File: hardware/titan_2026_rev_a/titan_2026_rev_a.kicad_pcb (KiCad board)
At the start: 2 copper layers, 65 x 56 mm, 73 parts, among them J1 SEC_{OUT}, J10 Conn_02x20_Odd_Even, J2 SEC_{IN}, J3 SWD, J4 BATTERY, J5 MONITOR, J6 DHT, J7 CO_{2}, J8 WHEELS, J9 USB_B_Mini, Q1 DMG2301L, SW1 RPON, SW2 SHTDN, SW3 MCU_RST, U1 NRF24L01, U2 AP62301WU, U3 ULT-GPS, U4 STM32F103C8Tx, Y1 8MHz

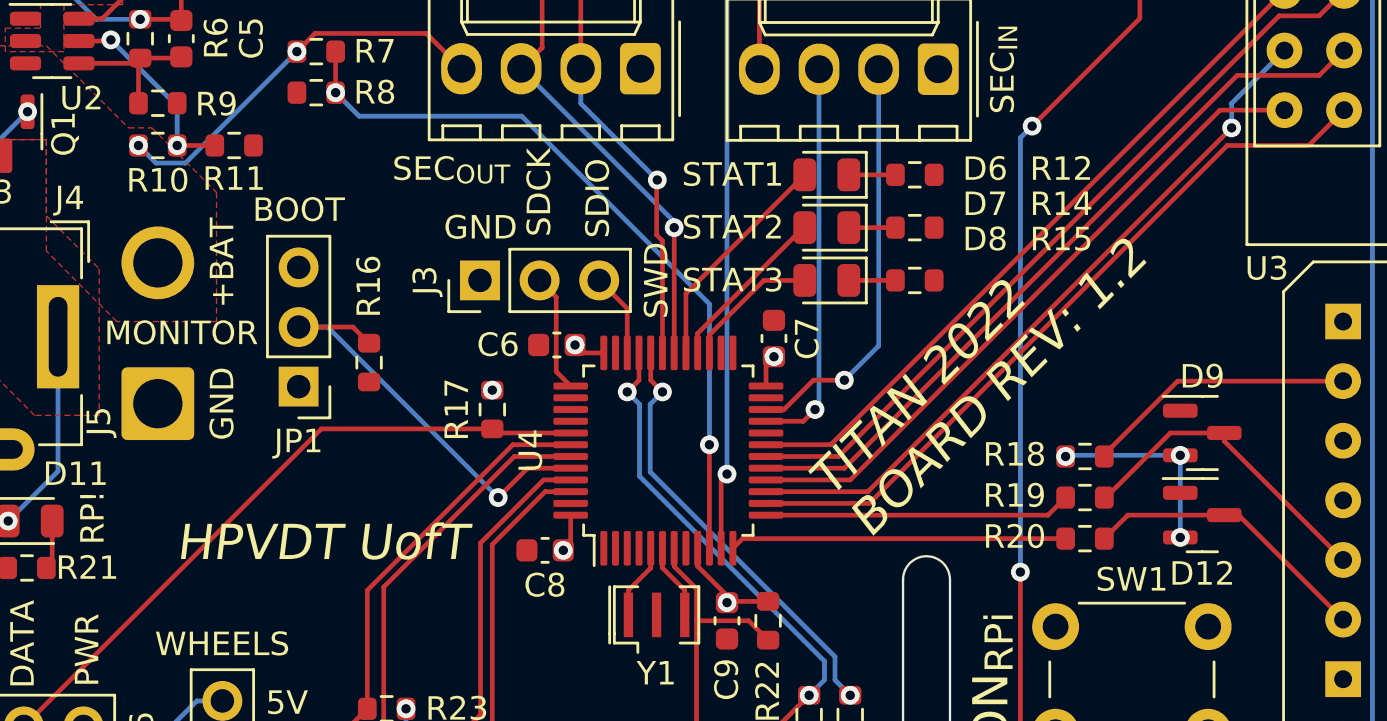
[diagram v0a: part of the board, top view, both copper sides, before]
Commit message: Brought KiCad projects into KiCad 10.0
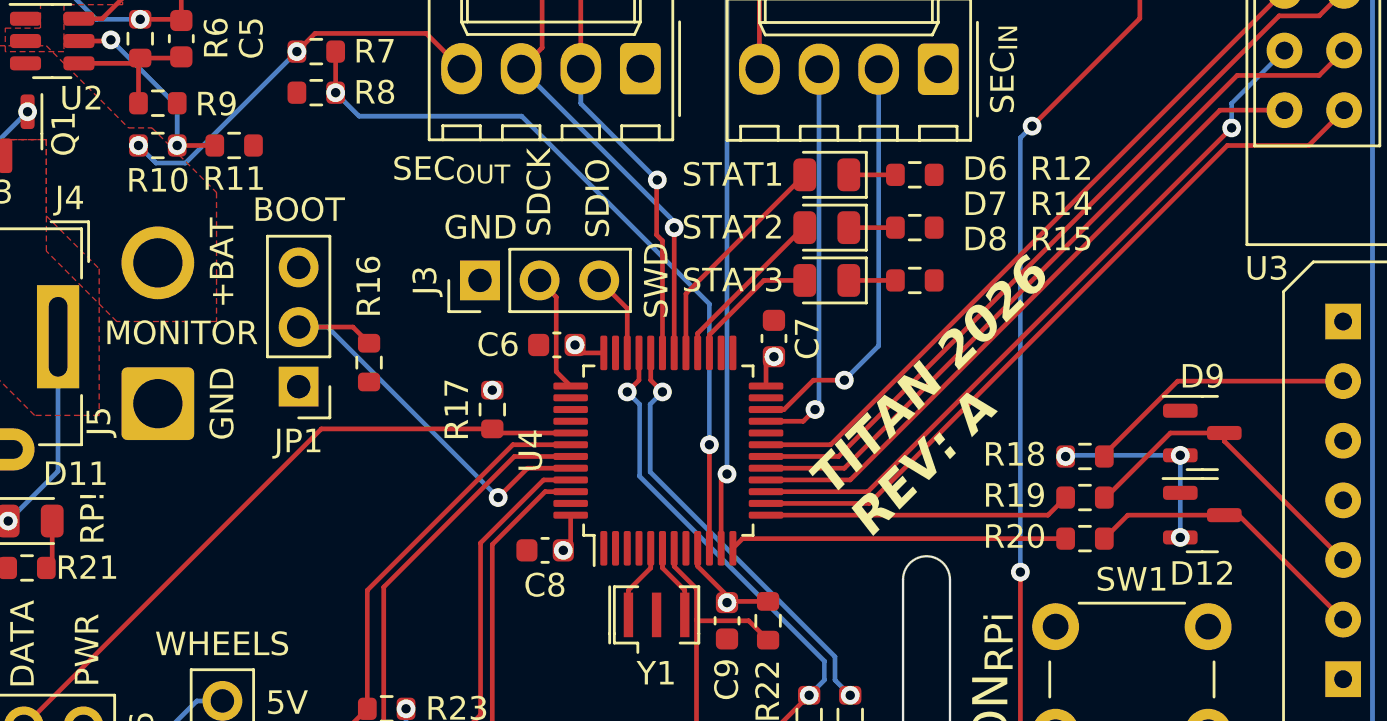
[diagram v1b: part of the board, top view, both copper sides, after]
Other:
- board text added: "TITAN 2026 REV: ${REVISION}"
- board text removed: "HPVDT UofT"
- board text removed: "TITAN 2022 BOARD REV: ${REVISION}"

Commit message: Completed rev A schematics
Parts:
- removed J5: MONITOR, Connector_Wire:SolderWire-1.5sqmm_1x02_P6mm_D1.7mm_OD3mm
- added BT1: Battery, Connector_AMASS:AMASS_XT30PW-M_1x02_P2.50mm_Horizontal, F.Cu at (120.0, 128.1)
- J4: value BATTERY -> Conn_01x02; footprint Connector_BarrelJack:BarrelJack_Wuerth_6941xx301002 -> Connector_AMASS:AMASS_XT30PW-F_1x02_P2.50mm_Horizontal
- moved J4 52.1 mm to (99.7, 129.1), turned to 0 degrees
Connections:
- J4 pad 1: /BATT_{IN+} -> GND
- J4 pad 2: GND -> +BATT

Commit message: Drafted initial floor plan of rev A
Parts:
- removed BT1: Battery, Connector_AMASS:AMASS_XT30PW-M_1x02_P2.50mm_Horizontal
- removed the C4 at (93.8, 65.3)
- removed the C5 at (103.0, 64.3)
- removed D10: BAV70, Package_TO_SOT_SMD:SOT-23
- removed D11: RP, Diode_SMD:D_0805_2012Metric
- removed D12, D9: TBAT54S, Package_TO_SOT_SMD:SOT-23
- removed D4, D6, D7, D8: LED, LED_SMD:LED_0805_2012Metric
- removed D5: 5V6, Diode_SMD:D_SOD-323
- removed the J1 at (122.6, 65.6)
- removed Q1: DMG2301L, Package_TO_SOT_SMD:SOT-23
- removed R25: 22, Resistor_SMD:R_0603_1608Metric
- removed R26: 2k, Resistor_SMD:R_0603_1608Metric
- removed R27: 10k, Resistor_SMD:R_0603_1608Metric
- removed SW2: SHTDN, Button_Switch_THT:SW_PUSH_6mm_H4.3mm
- removed SW3: MCU_RST, Button_Switch_THT:SW_PUSH_6mm_H4.3mm
- added C11: 100n, Capacitor_SMD:C_0402_1005Metric, F.Cu at (93.2, 65.5)
- added C12: 10u, Capacitor_SMD:C_0603_1608Metric, F.Cu at (118.0, 82.5)
- added C13: 100n, Capacitor_SMD:C_0402_1005Metric, F.Cu at (116.0, 87.8)
- added C14: 22u, Capacitor_SMD:C_0603_1608Metric, F.Cu at (127.5, 83.8)
- added C15: 22u, Capacitor_SMD:C_0603_1608Metric, F.Cu at (127.5, 87.2)
- added C16: 10u, Capacitor_SMD:C_0603_1608Metric, F.Cu at (105.5, 61.0)
- added C17: 10u, Capacitor_SMD:C_0603_1608Metric, F.Cu at (92.5, 74.5)
- added C18: 100n, Capacitor_SMD:C_0402_1005Metric, F.Cu at (89.5, 89.5)
- added C19: 470p, Capacitor_SMD:C_0402_1005Metric, F.Cu at (89.0, 94.5)
- added C20: 100n, Capacitor_SMD:C_0402_1005Metric, F.Cu at (123.0, 60.0)
- added C21: 100n, Capacitor_SMD:C_0402_1005Metric, F.Cu at (137.0, 60.0)
- added C22: 100n, Capacitor_SMD:C_0402_1005Metric, F.Cu at (109.5, 84.5)
- added C23: 100n, Capacitor_SMD:C_0402_1005Metric, F.Cu at (91.8, 59.5)
- added C8: 100n, Capacitor_SMD:C_0402_1005Metric, F.Cu at (111.8, 60.2)
- added C9: 100n, Capacitor_SMD:C_0402_1005Metric, F.Cu at (109.5, 87.5)
- added J10: XT30PW-F30.G.Y, Connector_AMASS:AMASS_XT30PW-F_1x02_P2.50mm_Horizontal, F.Cu at (129.0, 91.8)
- added J11: XT30PW-M30.G.Y, Connector_AMASS:AMASS_XT30PW-M_1x02_P2.50mm_Horizontal, F.Cu at (108.2, 92.8)
- added J12: BWSMA-KWE-Z001, Connector_Coaxial:SMA_BAT_Wireless_BWSMA-KWE-Z001, F.Cu at (83.5, 94.5)
- added J5: B3B-XH, Connector_JST:JST_XH_B3B-XH-A_1x03_P2.50mm_Vertical, F.Cu at (149.0, 83.0)
- added JP2: SolderJumper_3_Open, Jumper:SolderJumper-3_P2.0mm_Open_TrianglePad1.0x1.5mm, F.Cu at (110.2, 78.2)
- added JP3: SolderJumper_3_Open, Jumper:SolderJumper-3_P2.0mm_Open_TrianglePad1.0x1.5mm_NumberLabels, F.Cu at (119.5, 102.2)
- added JP4: SolderJumper_2_Open, Jumper:SolderJumper-2_P1.3mm_Open_Pad1.0x1.5mm, F.Cu at (130.0, 71.0)
- added L2: 6n8, Inductor_SMD:L_0402_1005Metric, F.Cu at (91.0, 94.0)
- added U10: TPS2116DRL, Package_TO_SOT_SMD:SOT-583-8, F.Cu at (130.7, 86.0)
- added U11: ATGM336H-5N31, titan:ATGM336H-5N, F.Cu at (95.5, 82.0)
- added U12: NRF24L01_Breakout, titan:nRF24L01_PA_LNA_Breakout, F.Cu at (103.0, 60.0)
- added U13: AT2659S, Package_TO_SOT_SMD:SOT-23-6, F.Cu at (92.0, 90.5)
- added U5: USBLC6-2SC6, Package_TO_SOT_SMD:SOT-23-6, F.Cu at (141.5, 95.0)
- added U6: INA219AIDCN, Package_SO:SOIC-8_3.9x4.9mm_P1.27mm, F.Cu at (105.0, 86.0)
- added U7: TLV73333PDBV, Package_TO_SOT_SMD:SOT-23-5, F.Cu at (91.8, 62.5)
- added U8: TPS563201, Package_TO_SOT_SMD:SOT-23-6, F.Cu at (117.0, 85.2)
- added U9: TPS2116DRL, Package_TO_SOT_SMD:SOT-583-8, F.Cu at (93.5, 67.5)
- C1: footprint Capacitor_SMD:C_0603_1608Metric -> Capacitor_SMD:C_0402_1005Metric
- C2, C3: value 22u -> 100n; footprint Capacitor_SMD:C_0805_2012Metric -> Capacitor_SMD:C_0402_1005Metric
- C4: renamed from C8; footprint Capacitor_SMD:C_0603_1608Metric -> Capacitor_SMD:C_0402_1005Metric
- C5: renamed from C6; footprint Capacitor_SMD:C_0603_1608Metric -> Capacitor_SMD:C_0402_1005Metric
- C6: renamed from C7; footprint Capacitor_SMD:C_0603_1608Metric -> Capacitor_SMD:C_0402_1005Metric
- C7: renamed from C9; footprint Capacitor_SMD:C_0603_1608Metric -> Capacitor_SMD:C_0402_1005Metric
- D1: value TBAT54S -> RED; footprint Package_TO_SOT_SMD:SOT-23 -> LED_SMD:LED_0805_2012Metric
- D2, D3: value TBAT54S -> WHITE; footprint Package_TO_SOT_SMD:SOT-23 -> LED_SMD:LED_0805_2012Metric
- J1: renamed from J10; value Conn_02x20_Odd_Even -> DS1023-2*20SF11
- J2: value SEC_{IN} -> B5B-XH; footprint Connector_Molex:Molex_KK-254_AE-6410-04A_1x04_P2.54mm_Vertical -> Connector_JST:JST_XH_B5B-XH-A_1x05_P2.50mm_Vertical
- J3: value SWD -> B5B-XH; footprint Connector_PinHeader_2.54mm:PinHeader_1x03_P2.54mm_Vertical -> Connector_JST:JST_XH_B5B-XH-A_1x05_P2.50mm_Vertical
- J4: value Conn_01x02 -> B3B-XH; footprint Connector_AMASS:AMASS_XT30PW-F_1x02_P2.50mm_Horizontal -> Connector_JST:JST_XH_B3B-XH-A_1x03_P2.50mm_Vertical
- J6: value DHT -> HB-PH9-12727PB2GOB; footprint Connector_PinHeader_2.54mm:PinHeader_1x03_P2.54mm_Vertical -> Connector_PinHeader_1.27mm:PinHeader_2x07_P1.27mm_Vertical_SMD
- J7: value CO_{2} -> B7B-XH; footprint Connector_PinHeader_2.54mm:PinHeader_1x03_P2.54mm_Vertical -> Connector_JST:JST_XH_B7B-XH-A_1x07_P2.50mm_Vertical
- J8: value WHEELS -> B7B-XH; footprint Connector_PinHeader_2.54mm:PinHeader_1x05_P2.54mm_Vertical -> Connector_JST:JST_XH_B7B-XH-A_1x07_P2.50mm_Vertical
- J9: value USB_B_Mini -> USB4105-GF-A-120; footprint 2172034-1:TE_2172034-1 -> Connector_USB:USB_C_Receptacle_GCT_USB4105-xx-A_16P_TopMnt_Horizontal
- JP1: value BOOT0 -> SolderJumper_3_Open; footprint Connector_PinHeader_2.54mm:PinHeader_1x03_P2.54mm_Vertical -> Jumper:SolderJumper-3_P2.0mm_Open_TrianglePad1.0x1.5mm
- L1: footprint Inductor_SMD:L_Taiyo-Yuden_NR-50xx -> Inductor_SMD:L_Changjiang_FNR6045S
- R1, R12, R14: value 330 -> 120; footprint Resistor_SMD:R_0603_1608Metric -> Resistor_SMD:R_0402_1005Metric
- R10: value 97k6 -> 5k1; footprint Resistor_SMD:R_0603_1608Metric -> Resistor_SMD:R_0402_1005Metric
- R11: value 13k3 -> 5k1; footprint Resistor_SMD:R_0603_1608Metric -> Resistor_SMD:R_0402_1005Metric
- R13: value 10k -> 10m; footprint Resistor_SMD:R_0603_1608Metric -> Resistor_SMD:R_0805_2012Metric
- R15: value 330 -> 2k; footprint Resistor_SMD:R_0603_1608Metric -> Resistor_SMD:R_0402_1005Metric
- R16, R17, R8, R9: value 10k -> 2k; footprint Resistor_SMD:R_0603_1608Metric -> Resistor_SMD:R_0402_1005Metric
- R18, R22, R3: value 10k -> 28k; footprint Resistor_SMD:R_0603_1608Metric -> Resistor_SMD:R_0402_1005Metric
- R19, R20: value 2k -> 5k1; footprint Resistor_SMD:R_0603_1608Metric -> Resistor_SMD:R_0402_1005Metric
- R2, R4: value 2k -> 120; footprint Resistor_SMD:R_0603_1608Metric -> Resistor_SMD:R_0402_1005Metric
- R21, R23: footprint Resistor_SMD:R_0603_1608Metric -> Resistor_SMD:R_0402_1005Metric
- R24: value 22 -> 2k; footprint Resistor_SMD:R_0603_1608Metric -> Resistor_SMD:R_0402_1005Metric
- R5: value 52k3 -> 5k1; footprint Resistor_SMD:R_0603_1608Metric -> Resistor_SMD:R_0402_1005Metric
- R6, R7: value 52k3 -> 2k; footprint Resistor_SMD:R_0603_1608Metric -> Resistor_SMD:R_0402_1005Metric
- SW1: value RPON -> SW_SPST; footprint Button_Switch_THT:SW_PUSH_6mm_H4.3mm -> titan:SW_SPST_SKPM
- U1: value NRF24L01 -> BME280; footprint RF_Module:nRF24L01_Breakout -> Package_LGA:Bosch_LGA-8_2.5x2.5mm_P0.65mm_ClockwisePinNumbering
- U2: value AP62301WU -> SCD41-D-R2; footprint Package_TO_SOT_SMD:TSOT-23-6 -> Sensor:Sensirion_SCD4x-1EP_10.1x10.1mm_P1.25mm_EP4.8x4.8mm
- U3: value ULT-GPS -> STM32F105RCT6; footprint ultimate_gps:ULT-GPS -> Package_QFP:LQFP-64_10x10mm_P0.5mm
- U4: value STM32F103C8Tx -> ISO1642DWR; footprint Package_QFP:LQFP-48_7x7mm_P0.5mm -> Package_SO:SOIC-16W_7.5x10.3mm_P1.27mm
- Y1: value 8MHz -> 8M; footprint Crystal:Resonator_SMD_Murata_CSTxExxV-3Pin_3.0x1.1mm -> Crystal:Crystal_SMD_2520-4Pin_2.5x2.0mm
- moved U1 85.4 mm to (76.2, 102.8), turned to 180 degrees
- moved SW1 65.9 mm to (84.0, 55.0), turned to 180 degrees
- moved J8 60.4 mm to (149.0, 61.5), turned to -90 degrees
- moved J4 58.2 mm to (140.9, 88.0), turned to 90 degrees
- moved J7 51.6 mm to (141.0, 76.5)
- moved J2 48.9 mm to (86.5, 62.0), turned to -90 degrees
- moved R11 48.3 mm to (144.5, 97.0)
- moved C1 47.2 mm to (75.2, 100.4), turned to 0 degrees
- moved R10 46.1 mm to (138.5, 97.0), turned to 0 degrees
- moved R23 45.2 mm to (153.0, 74.2), turned to -90 degrees
- moved J6 42.4 mm to (133.2, 78.2), turned to 0 degrees
- moved C2 40.4 mm to (77.2, 100.4), turned to 180 degrees
- moved R15 39.1 mm to (96.0, 66.5), turned to 0 degrees
- moved R22 38.0 mm to (153.0, 60.5)
- moved U3 37.9 mm to (115.2, 69.2), turned to -90 degrees
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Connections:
- C1 pad 1: /SW -> +3V3
- C1 pad 2: /BST -> GND
- C2 pad 1: +5V -> +3V3
- C3 pad 1: +5V -> GND
- C3 pad 2: GND -> +3V3
- D1 pad 2: +3V3 -> Net-(D1-A)
- D2 pad 2: +3V3 -> Net-(D2-A)
- D3 pad 2: +3V3 -> Net-(D3-A)
- J1 pad 1: +3V3 -> +3V3_RPI
- J1 pad 10: /GPIO15(RXD0) -> /RPI_{RX}
- J1 pad 15: unconnected-(J10-Pin_15-Pad15) -> /ROLE
- J1 pad 17: +3V3 -> +3V3_RPI
- J1 pad 37: /GPIO26 -> unconnected-(J1-GPIO26-Pad37)
- J1 pad 5: /GPIO3(SCL1) -> /RPI_SW
- J1 pad 8: /GPIO14(TXD0) -> /RPI_{TX}
- J2 pad 1: GND -> +5V
- J2 pad 2: /SEC_{TX} -> /SCL_{WHL}
- J2 pad 3: /SEC_{RX} -> /SDA_{WHL}
- J2 pad 4: /SEC_{BATT} -> /ENC_FRONT
- J3 pad 1: GND -> +5V
- J3 pad 2: /SWCLK -> /SCL_{WHL}
- J3 pad 3: /SDWIO -> /SDA_{WHL}
- J4 pad 1: GND -> +5V
- J4 pad 2: +BATT -> /CO_{2}
- J6 pad 1: GND -> unconnected-(J6-NC-Pad1)
- J6 pad 2: /DHT_{DATA} -> unconnected-(J6-NC-Pad2)
- J7 pad 1: GND -> /Interboard Comms/SCL_{ISO}
- J7 pad 2: /CO_{2} -> /Interboard Comms/SDA_{ISO}
- J7 pad 3: +5V -> /Interboard Comms/3V3_{ISO}
- J8 pad 1: GND -> /RPI_{TX}
- J8 pad 2: /ENCODER -> /RPI_{RX}
- J8 pad 3: /SDA -> /ROLE
- J8 pad 4: /SCL -> GND
- J8 pad 5: +5V -> +3V3
- JP1 pad 1: GND -> /SCL
- JP1 pad 2: /BOOT0 -> /Power/SDA
- JP1 pad 3: +3V3 -> /SCL_{SEC}
- L1 pad 1: /SW -> Net-(U8-SW)
- L1 pad 2: +5V -> /Power/5V_REG
- R1 pad 1: GND -> Net-(D1-A)
- R1 pad 2: Net-(D4-K) -> /STATUS_{1}
- R10 pad 1: /EN_{5V} -> GND
- R10 pad 2: +BATT -> Net-(J9-CC1)
- R11 pad 2: /EN_{5V} -> Net-(J9-CC2)
- R12 pad 1: GND -> Net-(J11-Pin_2)
- R13 pad 1: GND -> Net-(J11-Pin_2)
- R13 pad 2: /RP_{G} -> +BATT
- R14 pad 1: GND -> +BATT
- R15 pad 1: GND -> +3V3_RPI
- R15 pad 2: Net-(D8-K) -> Net-(R15-Pad2)
- R16 pad 1: GND -> Net-(R15-Pad2)
- R16 pad 2: /BOOT0 -> Net-(U9-PR1)
- R17 pad 1: /DHT_{DATA} -> Net-(U9-PR1)
- R17 pad 2: +3V3 -> GND
- R18 pad 1: /GPS_{EN} -> /Power/5V_REG
- R18 pad 2: +3V3 -> Net-(U8-VFB)
- R19 pad 1: /GPS_{TX} -> GND
- R19 pad 2: /GPS_{tx} -> Net-(U8-VFB)
- R2 pad 1: /RPI_{RX} -> Net-(D2-A)
- R2 pad 2: /GPIO15(RXD0) -> /STATUS_{2}
- R20 pad 1: /GPS_{RX} -> Net-(U10-PR1)
- R20 pad 2: /GPS_{rx} -> /Power/5V_REG
- R21 pad 1: Net-(D10-K) -> Net-(U10-PR1)
- R21 pad 2: Net-(D11-A) -> GND
- R22 pad 1: /RST -> /ROLE
- R22 pad 2: +3V3 -> GND
- R23 pad 1: +5V -> +3V3
- R23 pad 2: /SCL -> /SDA_{SEC}
- R24 pad 1: /D+ -> +3V3
- R24 pad 2: /d+ -> /SCL_{SEC}
- R3 pad 1: GND -> +3V3
- R3 pad 2: /SEC_{LVL} -> /~{RST}
- R4 pad 1: /RPI_{TX} -> Net-(D3-A)
- R4 pad 2: /GPIO14(TXD0) -> /STATUS_{3}
- R5 pad 1: /SEC_{LVL} -> /DHT_{DATA}
- R5 pad 2: /SEC_{BATT} -> +3V3
- R6 pad 1: /FEEDBACK -> +5V
- R6 pad 2: +5V -> /SCL_{WHL}
- R7 pad 1: /BATT_{LVL} -> +5V
- R7 pad 2: +BATT -> /SDA_{WHL}
- R8 pad 1: GND -> +3V3
- R8 pad 2: /BATT_{LVL} -> /SCL
- R9 pad 1: GND -> +3V3
- R9 pad 2: /FEEDBACK -> /SDA
- SW1 pad 1: GND -> /RPI_SW
- SW1 pad 2: /GPIO3(SCL1) -> GND
- U1 pad 3: /RF_{EN} -> /SDA
- U1 pad 4: /RF_{SEL} -> /SCL
- U1 pad 5: /SCK -> +3V3
- U1 pad 6: /MOSI -> +3V3
- U1 pad 7: /MISO -> GND
- U1 pad 8: /RF_{INT} -> +3V3
- U2 pad 1: GND -> (no net)
- U2 pad 2: /SW -> (no net)
- U2 pad 3: +BATT -> (no net)
- U2 pad 4: /FEEDBACK -> (no net)
- U2 pad 5: /EN_{5V} -> (no net)
- U2 pad 6: /BST -> GND
- U3 pad 1: unconnected-(U3-3V3_{INT}-Pad1) -> +3V3
- U3 pad 2: /GPS_{EN} -> unconnected-(U3-PC13-Pad2)
- U3 pad 4: unconnected-(U3-FIX-Pad4) -> /ROLE
- U3 pad 5: /GPS_{tx} -> Net-(U3-PD0)
- U3 pad 6: /GPS_{rx} -> unconnected-(U3-PD1-Pad6)
- U3 pad 7: GND -> /~{RST}
- U3 pad 8: +3V3 -> unconnected-(U3-PC0-Pad8)
- U4 pad 1: unconnected-(U4-VBAT-Pad1) -> +3V3
- U4 pad 10: /BATT_{LVL} -> unconnected-(U4-NC-Pad10)
- U4 pad 11: /SEC_{LVL} -> /Interboard Comms/SCL_{ISO}
- U4 pad 12: /GPS_{RX} -> /Interboard Comms/TX_{ISO}
- U4 pad 13: /GPS_{TX} -> /Interboard Comms/RX_{ISO}
- U4 pad 14: /RF_{INT} -> /Interboard Comms/SDA_{ISO}
- U4 pad 15: /SCK -> unconnected-(U4-NC-Pad15)
- U4 pad 16: /MISO -> /Interboard Comms/3V3_{ISO}
- U4 pad 3: unconnected-(U4-PC14-Pad3) -> /SDA
- U4 pad 4: unconnected-(U4-PC15-Pad4) -> /SEC_{RX}
- U4 pad 5: Net-(U4-PD0) -> /SEC_{TX}
- U4 pad 6: Net-(U4-PD1) -> /SCL
- U4 pad 7: /RST -> unconnected-(U4-NC-Pad7)
- U4 pad 9: +3V3 -> /Interboard Comms/GND_{ISO}
- Y1 pad 1: Net-(U4-PD0) -> +3V3
- Y1 pad 3: Net-(U4-PD1) -> Net-(U3-PD0)
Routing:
- net +5V: track 104.0 -> 0.00 mm, vias 6 -> 0
- net /GPIO3(SCL1): track 102.7 -> 0.00 mm
- net /GPIO26: track 57.7 -> 0.00 mm, vias 2 -> 0
- net /CO_{2}: track 34.8 -> 0.00 mm
- net /SEC_{LVL}: track 33.2 -> 0.00 mm, vias 2 -> 0
- net /RF_{SEL}: track 32.8 -> 0.00 mm
- net /MOSI: track 32.0 -> 0.00 mm
- net /BATT_{LVL}: track 31.8 -> 0.00 mm, vias 2 -> 0
- net /RF_{INT}: track 31.6 -> 0.00 mm
- net /SCK: track 30.5 -> 0.00 mm, vias 1 -> 0
- net /RF_{EN}: track 30.1 -> 0.00 mm
- net /DHT_{DATA}: track 28.6 -> 0.00 mm
- net /MISO: track 28.6 -> 0.00 mm
- net /ENCODER: track 26.4 -> 0.00 mm
- net /RST: track 25.2 -> 0.00 mm
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- removed copper zone on F.Cu, net +5V
- removed copper zone on F.Cu, net +BATT
- removed copper zone on F.Cu, net /BATT_{IN+}
- removed copper zone on F.Cu, net /SW
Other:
- board size 65 x 56 mm -> 82 x 56 mm
- board text added: "Avoiding heating from rest of PCB with rule block"
- board text added: "BATT"
- board text added: "FRNT"
- board text added: "GND TIE"
- board text added: "GPS"
- board text added: "PRIM"
- board text added: "PRIM_{IN}"
- board text added: "PWR_{RPi}"
- board text added: "REAR"
- board text added: "SEC"
- board text removed: "+BAT"
- board text removed: "- Encoder based speed/distance - GPS based speed/distance - Battery levels - CO_{2} levels - Brake temperatures - Ambient temp. / humidity - Rider cadence, heart rate, power"
- board text removed: "BOOT"
- board text removed: "Complete assembly needed only for main screen. Only power supply and {dblquote}SEC_{OUT}{dblquote} header needed on secondary HAT."
- board text removed: "DATA"
- board text removed: "Data collected:"
- board text removed: "JLCJLCJLCJLC"
- board text removed: "OFF_{RPi}"
- board text removed: "ON_{RPi}"
- board text removed: "PWR"
- board text removed: "RP!"
- board text removed: "RST_{MCU}"
- board text removed: "SB"
- board text removed: "SDCK"
- board text removed: "SDIO"
- board text removed: "SEC_{IN}"
- board text removed: "STM32 centered HAT for TITAN. Provides power from battery with UVLO and reverse polarity protection. All data on TITAN passes through the STM32 by UART. Telemetry provided by nRF24L01 module."
- board text removed: "SWD"
- board text removed: "Sec. SEC_{OUT} to main's SEC_{IN} pin-pin!"
- board text removed: "TITAN 2022 RPi HAT"
- board text removed: "TITAN 2026 REV: ${REVISION}"

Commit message: Completed initial layout of rev A
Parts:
- removed H1, H2, H3, H4: M2.5, MountingHole:MountingHole_2.7mm_M2.5
- added MH1: MountingHole_2.7mm_M2.5_ISO14580_Pad_TopBottom, MountingHole:MountingHole_2.7mm_M2.5_ISO14580_Pad_TopBottom, F.Cu at (93.2, 53.8)
- added MH3: MountingHole_2.7mm_M2.5_ISO14580_Pad_TopBottom, MountingHole:MountingHole_2.7mm_M2.5_ISO14580_Pad_TopBottom, F.Cu at (93.2, 102.8)
- added MH4: MountingHole_2.7mm_M2.5_ISO14580_Pad_TopBottom, MountingHole:MountingHole_2.7mm_M2.5_ISO14580_Pad_TopBottom, F.Cu at (151.2, 102.8)
- added MH4: MountingHole_2.7mm_M2.5_ISO14580_Pad_TopBottom, MountingHole:MountingHole_2.7mm_M2.5_ISO14580_Pad_TopBottom, F.Cu at (151.2, 53.8)
- moved C1 7.50 mm to (75.5, 92.9)
- moved C2 7.50 mm to (77.5, 92.9)
- moved U1 7.50 mm to (76.5, 95.2)
- moved R19 2.00 mm to (113.8, 84.2), turned to 0 degrees
- moved R11 1.00 mm to (145.5, 97.0)
- moved R10 0.99 mm to (137.5, 97.0)
- moved C12 0.80 mm to (118.2, 81.8), turned to 90 degrees
- moved C6 0.53 mm to (120.8, 75.5)
- moved C5 0.42 mm to (121.5, 63.5)
- moved R18 0.34 mm to (115.5, 82.8), turned to 180 degrees
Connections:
- JP1 pad 1: /SCL -> /SDA
- JP1 pad 3: /SCL_{SEC} -> /SDA_{SEC}
- JP2 pad 1: /SDA -> /SCL
- JP2 pad 3: /SDA_{SEC} -> /SCL_{SEC}
- U3 pad 16: /GPS_{RX} -> /RPI_{RX}
- U3 pad 17: /GPS_{TX} -> /RPI_{TX}
- U3 pad 24: /RF_{EN} -> /RF_{INT}
- U3 pad 25: /RF_{INT} -> /RF_{EN}
- U3 pad 42: /VCP_TX -> /GPS_{RX}
- U3 pad 43: /VCP_RX -> /GPS_{TX}
- U3 pad 51: /SEC_{RX} -> /VCP_TX
- U3 pad 52: /SEC_{TX} -> /VCP_RX
- U3 pad 53: /RPI_{RX} -> /SEC_{RX}
- U3 pad 54: /RPI_{TX} -> /SEC_{TX}
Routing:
- net +5V: track 0.00 -> 129.0 mm, vias 0 -> 3
- net +3V3: track 1.48 -> 106.4 mm, vias 0 -> 12
- net /ROLE: track 0.00 -> 89.7 mm, vias 0 -> 5
- net /SDA: track 0.00 -> 82.9 mm, vias 0 -> 4
- net /SCL: track 0.00 -> 79.9 mm, vias 0 -> 4
- net /RPI_{TX}: track 0.00 -> 65.8 mm
- net /RPI_{RX}: track 0.00 -> 62.9 mm
- net /SCL_{WHL}: track 0.00 -> 54.7 mm, vias 0 -> 1
- net /ENC_REAR: track 0.00 -> 53.2 mm, vias 0 -> 2
- net /SCL_{SEC}: track 0.00 -> 46.4 mm, vias 0 -> 3
- net /SDA_{SEC}: track 0.00 -> 46.1 mm, vias 0 -> 3
- net /SDA_{WHL}: track 0.00 -> 45.2 mm, vias 0 -> 2
- net /DHT_{DATA}: track 0.00 -> 45.0 mm, vias 0 -> 2
- net /Interboard Comms/GND_{ISO}: track 0.00 -> 40.5 mm
- net /~{RST}: track 0.00 -> 37.0 mm, vias 0 -> 2
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- added copper zone on B.Cu, net +5V
- added copper zone on F.Cu, net /Power/5V_REG
- added copper zone on F.Cu, net Net-(J11-Pin_2)
- added copper zone on F.Cu, net Net-(U8-SW)
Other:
- outline, holes or cut-outs redrawn
- board text added: "Avoiding heat from rest of PCB to sensor with rule block"
- board text added: "TITAN 2026 REV. ${REVISION}"
- board text removed: "Avoiding heating from rest of PCB with rule block"
